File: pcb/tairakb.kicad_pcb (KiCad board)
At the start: 2 copper layers, 151.5 x 121.2 mm, 79 parts, among them SW1 SW_Push, SW10 SW_Push, SW11 SW_Push, SW12 SW_Push, SW13 SW_Push, SW14 SW_Push, SW15 SW_Push, SW16 SW_Push, SW17 SW_Push, SW18 SW_Push, SW19 SW_Push, SW2 SW_Push, SW20 SW_Push, SW20-1 SW_Push, SW21 SW_Push, SW22 SW_Push, SW23 SW_Push, SW24 SW_Push, SW25 SW_Push, SW26 SW_Push, SW27 SW_Push, SW28 SW_Push, SW29 SW_Push, SW3 SW_Push, SW30 SW_Push, SW31 SW_Push, SW32 SW_Push, SW33 SW_Push, SW4 SW_Push, SW5 SW_Push, SW6 SW_Push, SW7 SW_Push, SW8 SW_Push, SW9 SW_Push, U3 nice!nano

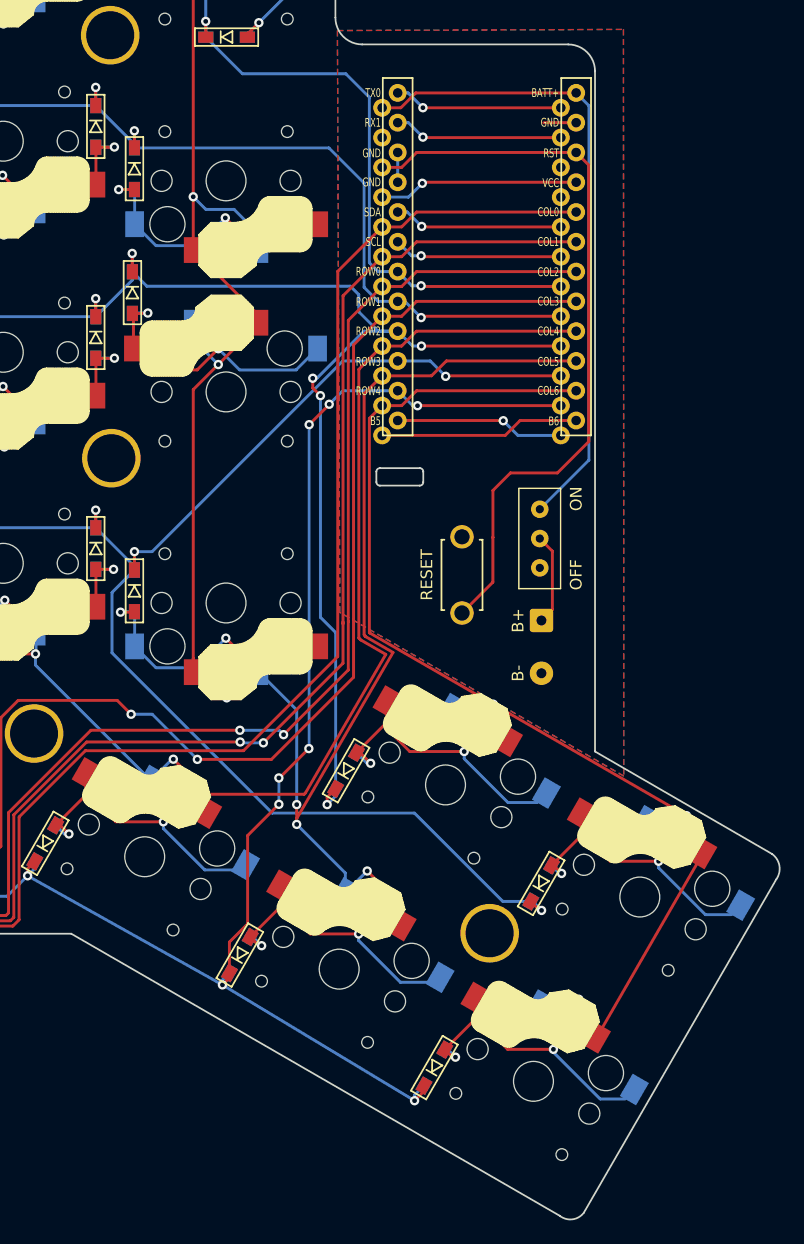
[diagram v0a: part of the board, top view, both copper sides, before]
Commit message: remove outermost two thumb keys (SW32, SW33)
Shrinks the thumb cluster from 5 to 3 keys (SW25, SW30, SW31 remain).
Deletes the footprints, schematic symbols, orphan D32/D33-Pad2 traces,
and the dangling /col6 segments/vias in the cut region; trims Edge.Cuts
on the PCB and both plates to wrap only the remaining keys (H8 stays
enclosed). DRC stays at the pre-existing 4-violation baseline; ERC
clean.

Co-Authored-By: Claude Opus 4.7 <noreply@anthropic.com>
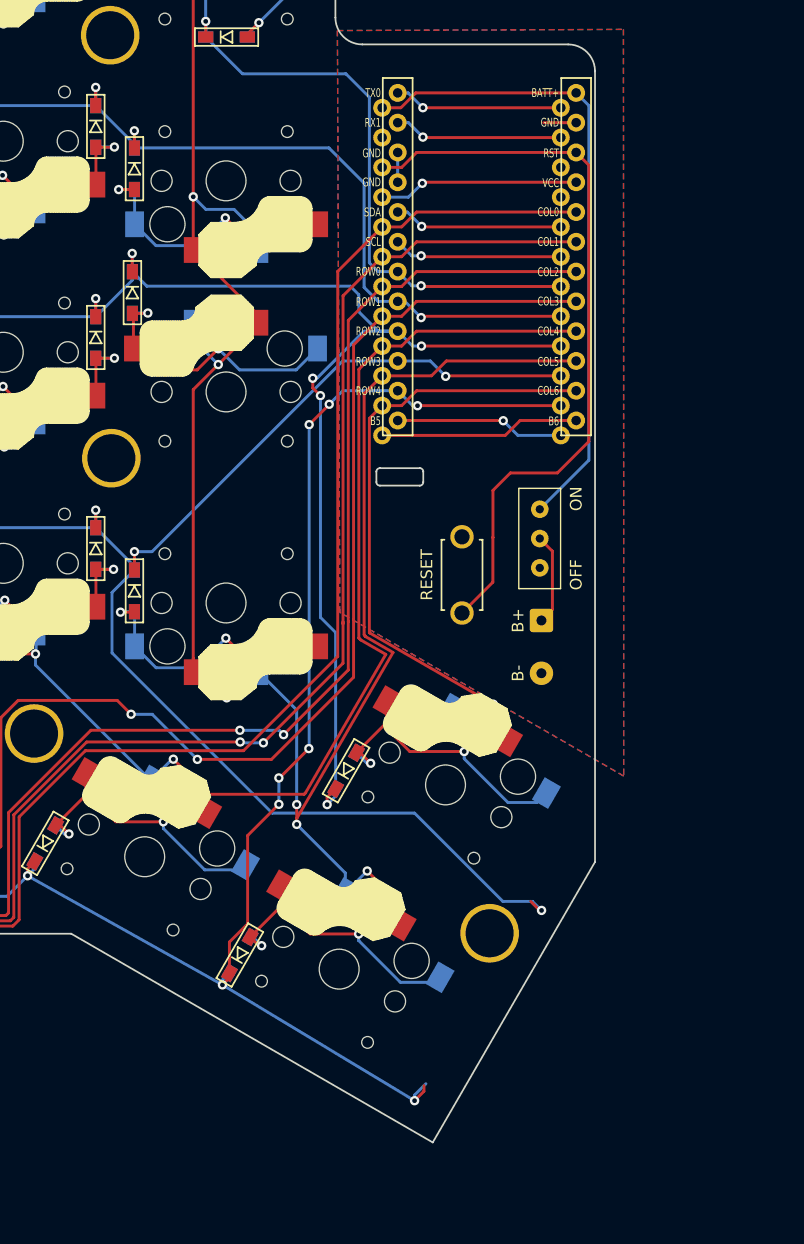
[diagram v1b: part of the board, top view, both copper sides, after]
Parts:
- removed D32, D33: D, tairakb:D3_SMD
- removed SW32, SW33: SW_Push, tairakb:Choc_Hotswap
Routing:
- net /col6: track 108.9 -> 56.8 mm, vias 3 -> 1
- net Net-(D32-Pad2): track 26.6 -> 0.00 mm, vias 2 -> 0
- net Net-(D33-Pad2): track 26.5 -> 0.00 mm, vias 2 -> 0
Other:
- board size 151.5 x 121.2 mm -> 135.8 x 114.6 mm

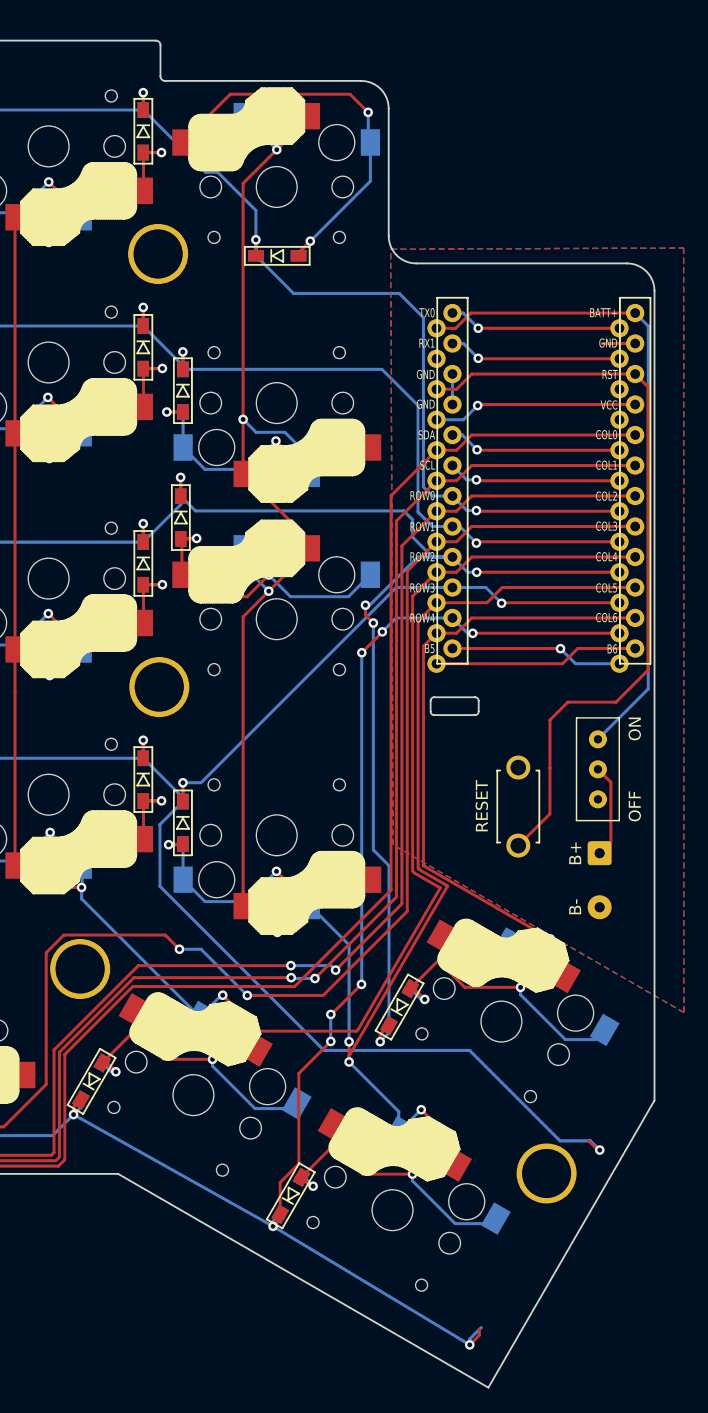
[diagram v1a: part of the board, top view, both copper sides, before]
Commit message: 1.5U bottom thumb + thumb cluster reflow (Pass A)
SW30 enlarged to 1.5U using a new Choc_Hotswap_1.5U footprint (no
stabilizers); the keycap's bottom edges are anchored, so the switch
center shifts up-and-right to (194.515, 133.274). SW31 rotated from
-30° to 180° and placed beside SW29 in the next main-grid column at
(201.295, 106.594). U3 moved up to (204.445, 61.112) so its top edge
aligns with SW26; PCB and both plate Edge.Cuts extended in the
controller area to give U3 the needed vertical room. RSW1, BSW1, BT1
shifted up 15mm to clear the new SW31 and U3 envelopes. Schematic
SW30 footprint property updated to match.

Pass A only: trace endpoints near moved pads have been nudged or, for
SW31's deleted pad stubs, removed. Broader re-routing in KiCad GUI is
pending and will land in a follow-up commit; DRC currently reports
~495 violations in the affected region.

Co-Authored-By: Claude Opus 4.7 <noreply@anthropic.com>
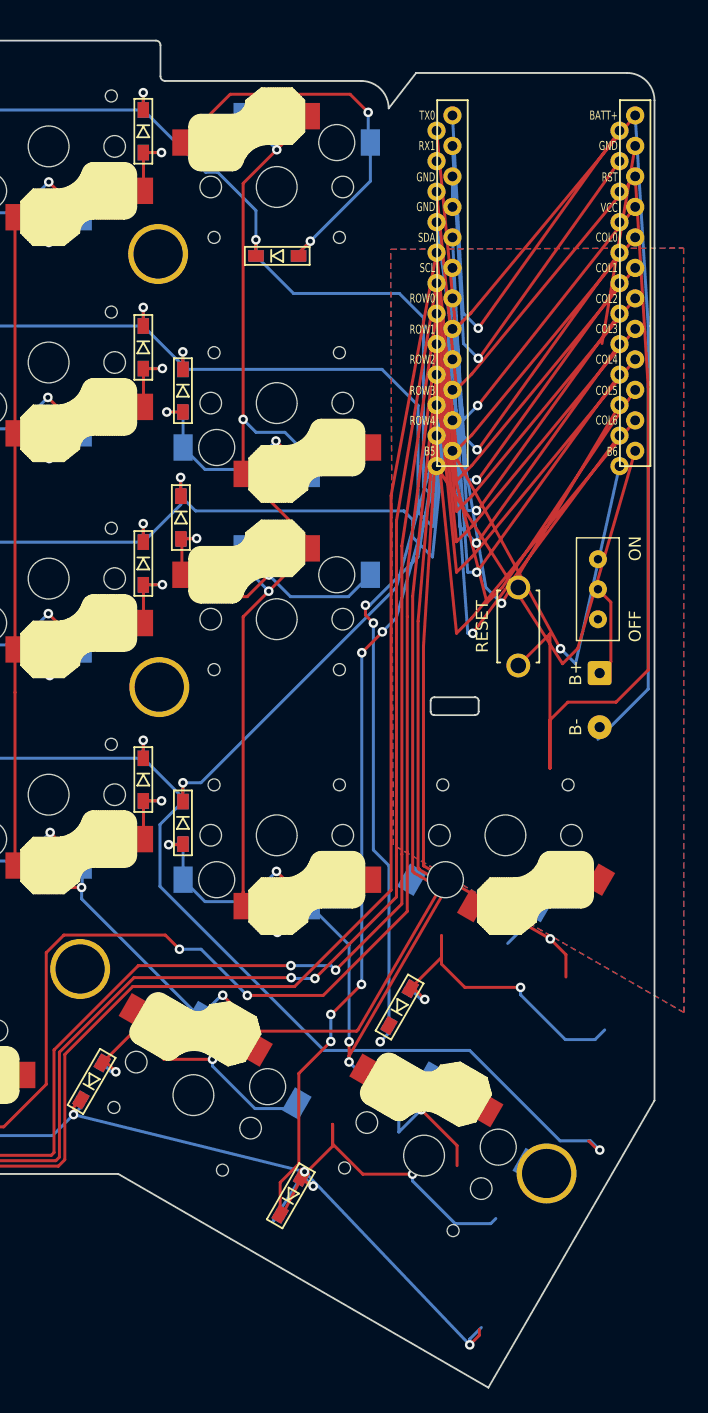
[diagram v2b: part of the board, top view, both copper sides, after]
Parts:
- SW30: footprint tairakb:Choc_Hotswap -> tairakb:Choc_Hotswap_1.5U
- moved U3 16.5 mm to (204.4, 61.1)
- moved SW31 15.5 mm to (201.3, 106.6), turned to 180 degrees
- moved BSW1 15.0 mm to (209.0, 88.6)
- moved BT1 15.0 mm to (209.1, 93.1)
- moved RSW1 15.0 mm to (202.4, 89.2)
- moved SW30 5.25 mm to (194.5, 133.3)
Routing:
- net /row2: track 192.1 -> 243.5 mm
- net /row4: track 215.7 -> 262.1 mm
- net /RST: track 63.6 -> 109.7 mm
- net /row0: track 162.3 -> 201.6 mm
- net /row1: track 151.0 -> 190.2 mm
- net +BATT: track 54.8 -> 93.5 mm
- net /col4: track 175.1 -> 213.5 mm
- net /col3: track 226.8 -> 265.1 mm
- net /col2: track 248.3 -> 286.4 mm
- net /col1: track 269.1 -> 307.0 mm
- net /col0: track 283.2 -> 321.1 mm
- net /col5: track 188.1 -> 225.6 mm
- net /col6: track 56.8 -> 92.6 mm
- net /row3: track 201.9 -> 237.6 mm
- net Net-(U3-Pad6): track 14.4 -> 38.9 mm
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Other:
- outline, holes or cut-outs redrawn
